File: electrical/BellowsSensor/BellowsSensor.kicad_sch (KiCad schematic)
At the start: 5 parts, among them J1 I2C, U1 ELVH-001D-HRRJ-C-N2A4

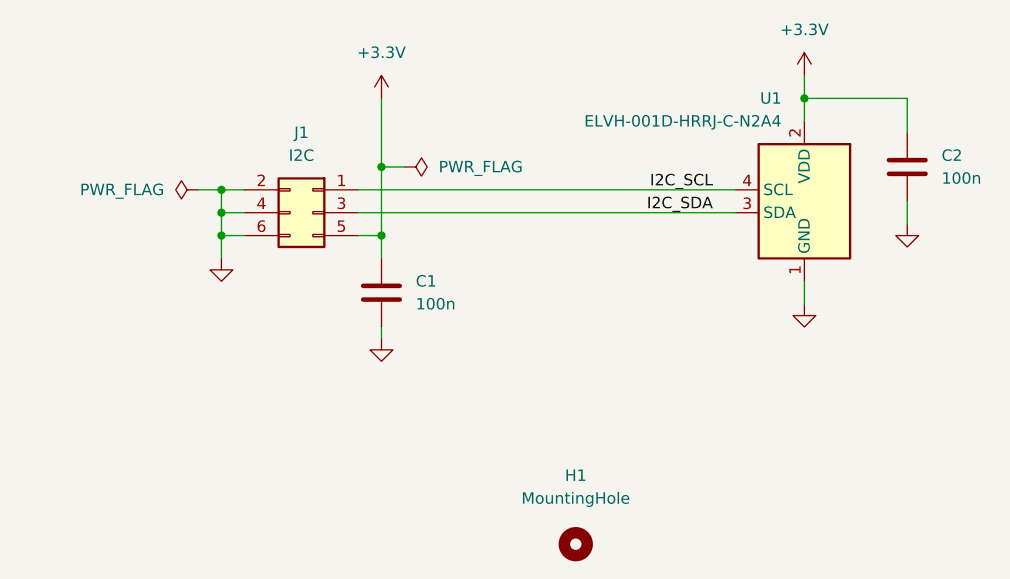
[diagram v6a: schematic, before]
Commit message: Change i2c cable pinout to keep signals between grounds
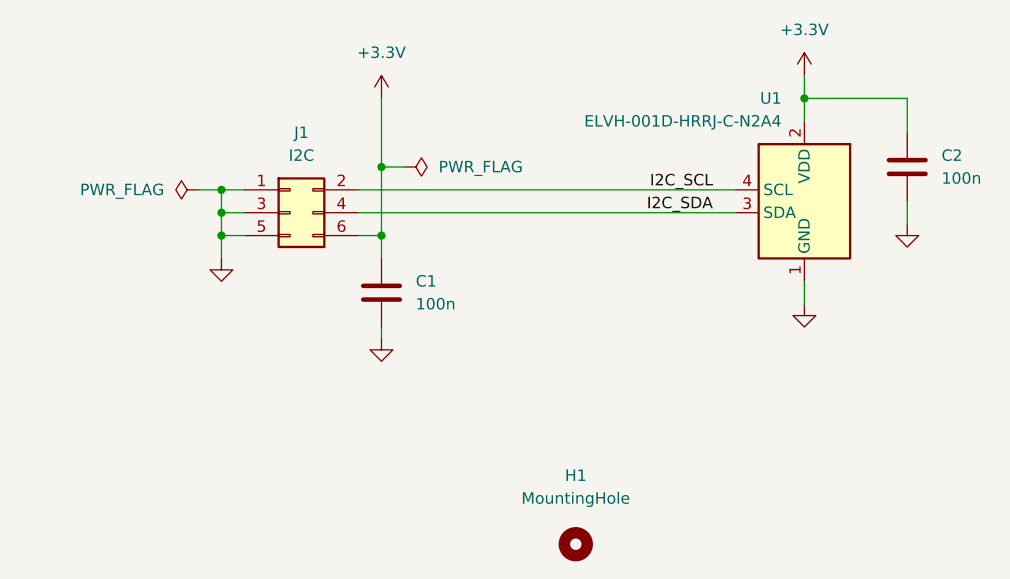
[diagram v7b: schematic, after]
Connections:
- net +3.3V: now also J1.6 (Pin_6); no longer J1.5 (Pin_5)
- net GND: now also J1.1 (Pin_1), J1.3 (Pin_3), J1.5 (Pin_5); no longer J1.2 (Pin_2), J1.4 (Pin_4), J1.6 (Pin_6)
- net I2C_SCL: now also J1.2 (Pin_2); no longer J1.1 (Pin_1)
- net I2C_SDA: now also J1.4 (Pin_4); no longer J1.3 (Pin_3)
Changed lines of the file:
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@@
 	(symbol
 		(lib_id "Connector_Generic:Conn_02x03_Odd_Even")
-		(at 104.14 80.01 0)
-		(mirror y)
+		(at 101.6 80.01 0)
 		(unit 1)
 		(exclude_from_sim no)
@@
 		(on_board yes)
 		(dnp no)
-		(fields_autoplaced yes)
 		(property "Reference" "J1"
 			(at 102.87 71.12 0)
@@
 		)
 		(property "Footprint" "MidiConcertina:Wuerth_WR-WST_490107670612_2x03_P2.54mm_SKEDD"
-			(at 104.14 80.01 0)
+			(at 101.6 80.01 0)
 			(effects
 				(font
@@
 		)
 		(property "Datasheet" ""
-			(at 104.14 80.01 0)
+			(at 101.6 80.01 0)
 			(effects
 				(font
@@
 		)
 		(property "Description" ""
-			(at 104.14 80.01 0)
+			(at 101.6 80.01 0)
 			(effects
 				(font
